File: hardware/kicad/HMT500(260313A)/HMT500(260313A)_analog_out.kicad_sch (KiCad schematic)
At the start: 35 parts, among them U10 TPS26611DDFR, U12 OPA197IDBVR, U13 OPA197IDBVR, U14 SN74LVC2G32DCUR, U7 DAC8760IPWP, U8 DAC8760IPWP, U9 TPS26611DDFR

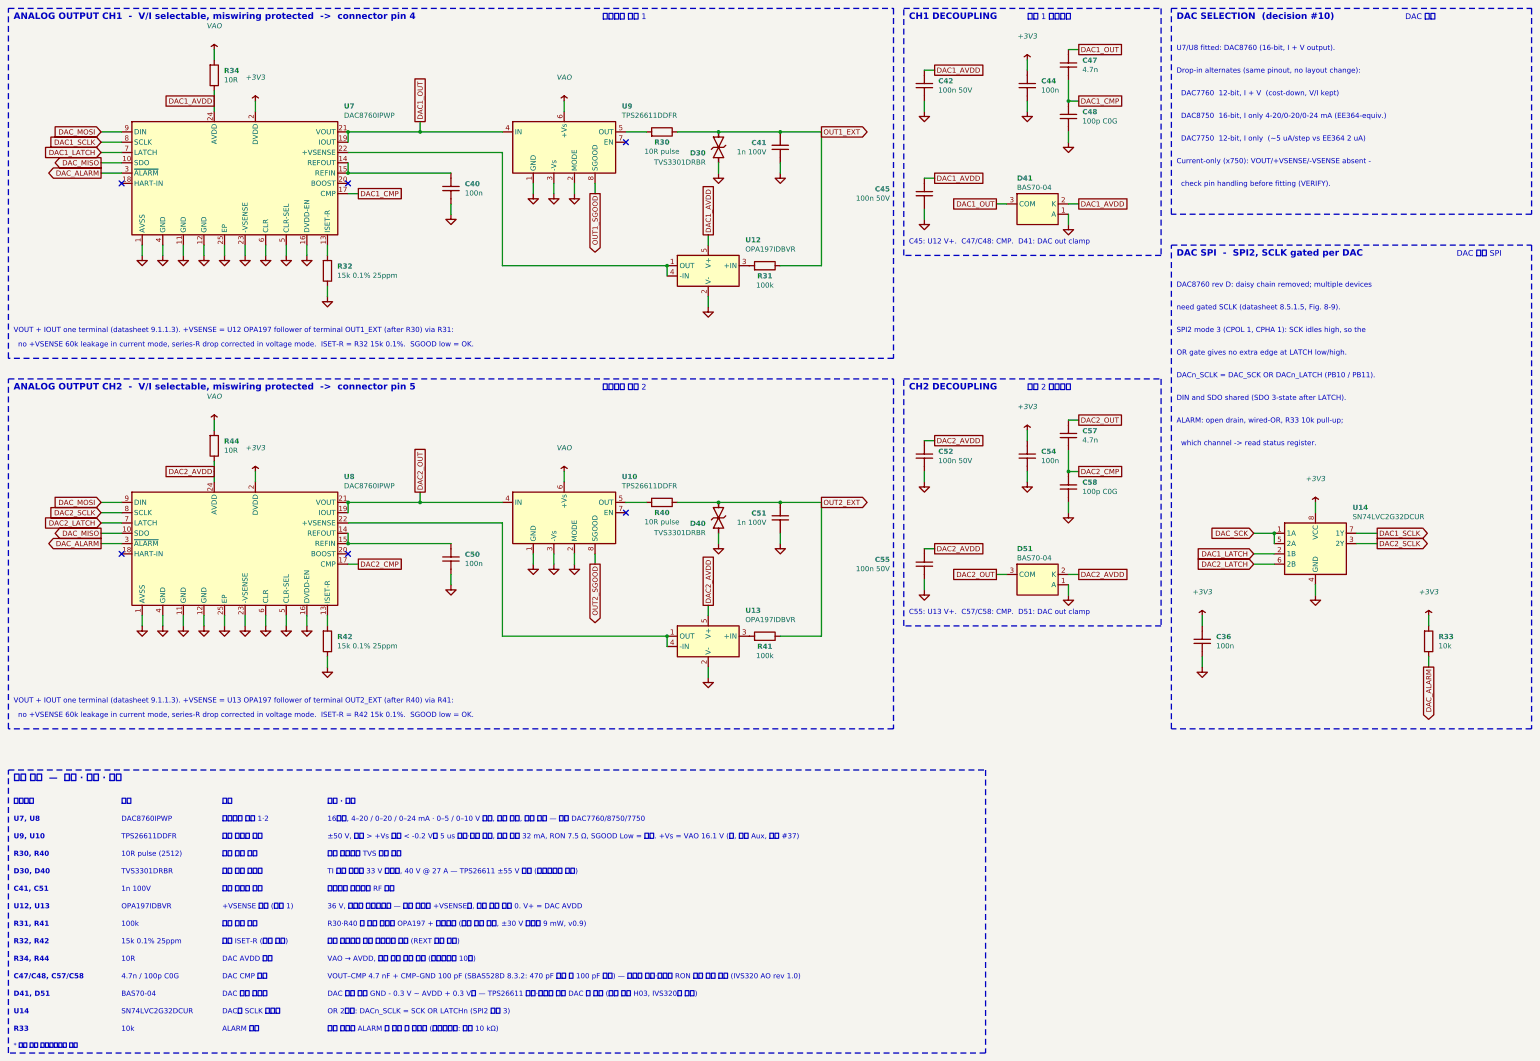
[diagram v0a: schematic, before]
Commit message: 회로 v0.10: AO D30/D40을 TVS1401 14 V로 변경
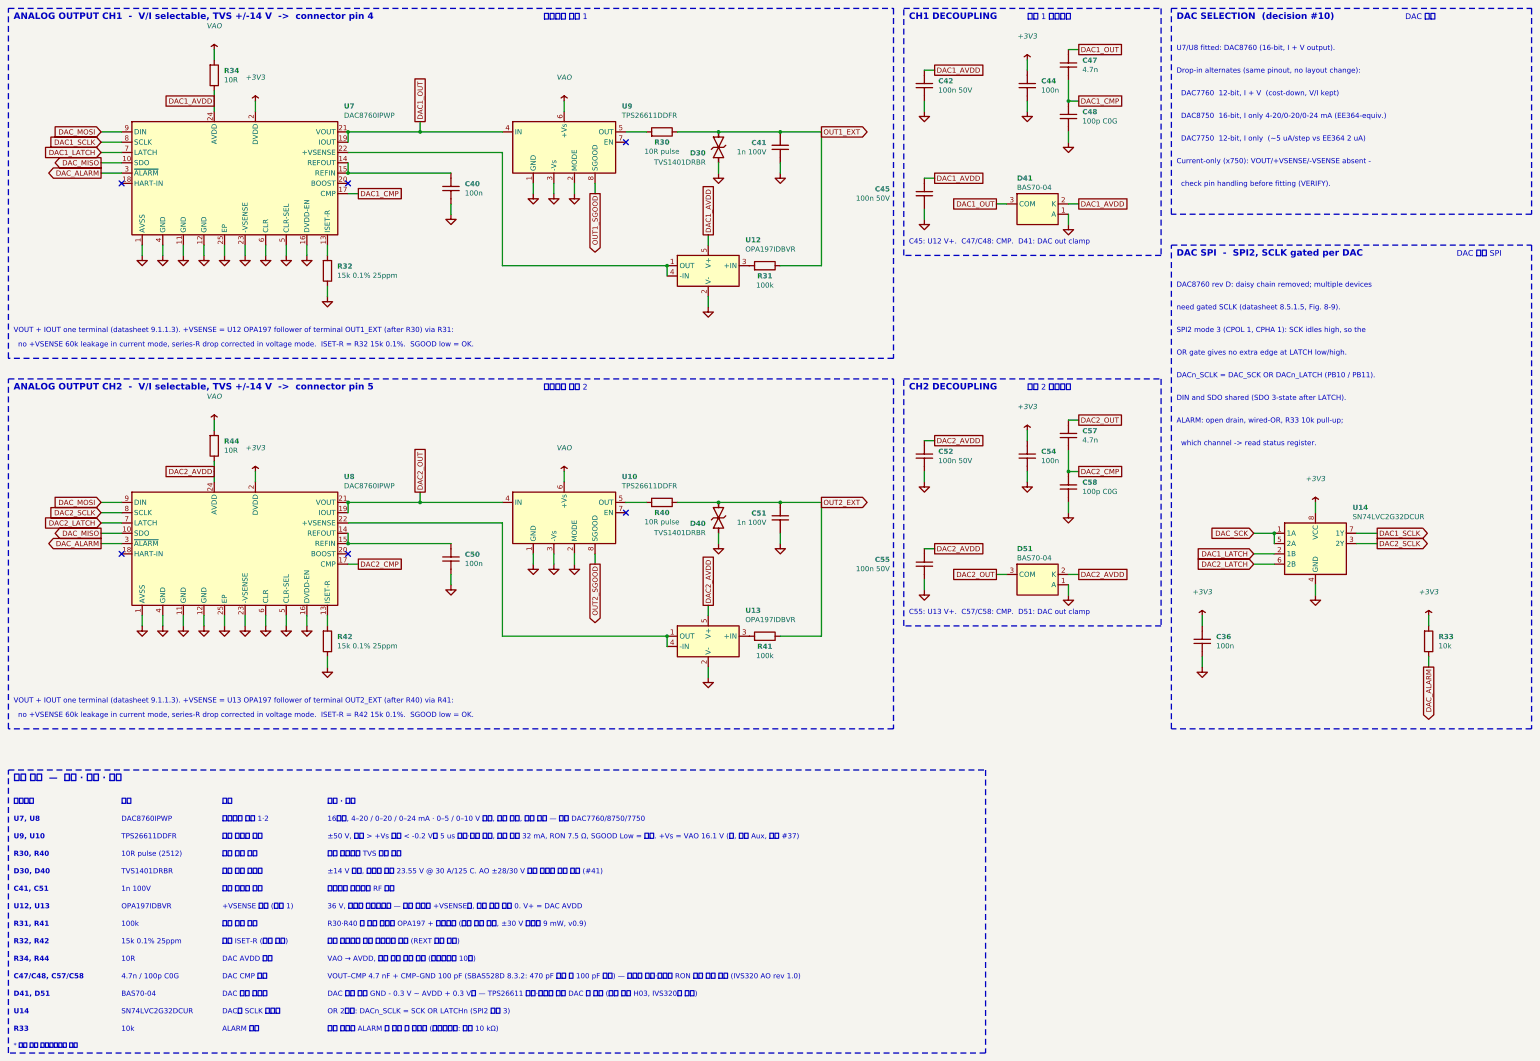
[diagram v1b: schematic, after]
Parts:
- D30, D40: value TVS3301DRBR -> TVS1401DRBR; symbol HMT500_260313A:TVS3301 -> HMT500_260313A:TVS1401
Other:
- note added: "ANALOG OUTPUT CH1 - V/I selectable, TVS +/-14 V -> connector pin 4"
- note added: "ANALOG OUTPUT CH2 - V/I selectable, TVS +/-14 V -> connector pin 5"
- note added: "TVS1401DRBR"
- note added: "±14 V 동작, 클램프 최대 23.55 V @ 30 A/125 C. AO ±28/30 V 지속 오결선 보장 제외 (#41)"
- note removed: "ANALOG OUTPUT CH1 - V/I selectable, miswiring protected -> connector pin 4"
- note removed: "ANALOG OUTPUT CH2 - V/I selectable, miswiring protected -> connector pin 5"
- note removed: "TI 평탄 클램프 33 V 양방향, 40 V @ 27 A — TPS26611 ±55 V 보호 (데이터시트 권장)"
- note removed: "TVS3301DRBR"

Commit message: Add HMT500 A1 routing draft and correct SMNR4020 land patterns
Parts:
- C36, C40, C44, C47, C48, C50, C54, C57, C58: footprint Capacitor_SMD:C_0402_1005Metric -> HMT500_260313A:C_0402_1005Metric
- C41, C51: footprint Capacitor_SMD:C_0603_1608Metric -> HMT500_260313A:C_0603_1608Metric
- C42, C45, C52, C55: footprint Capacitor_SMD:C_0805_2012Metric -> HMT500_260313A:C_0805_2012Metric
- D41, D51: footprint Package_TO_SOT_SMD:SOT-23 -> HMT500_260313A:SOT-23
- R30, R40: footprint Resistor_SMD:R_2512_6332Metric -> HMT500_260313A:R_2512_6332Metric
- R31, R33, R34, R41, R44: footprint Resistor_SMD:R_0402_1005Metric -> HMT500_260313A:R_0402_1005Metric
- R32, R42: footprint Resistor_SMD:R_0603_1608Metric -> HMT500_260313A:R_0603_1608Metric
- U10, U9: footprint Package_TO_SOT_SMD:SOT-23-8 -> HMT500_260313A:SOT-23-8
- U12, U13: footprint Package_TO_SOT_SMD:SOT-23-5 -> HMT500_260313A:SOT-23-5
- U14: footprint Package_SO:VSSOP-8_2.3x2mm_P0.5mm -> HMT500_260313A:VSSOP-8_2.3x2mm_P0.5mm
- U7, U8: footprint Package_SO:HTSSOP-24-1EP_4.4x7.8mm_P0.65mm_EP3.2x5mm -> HMT500_260313A:HTSSOP-24-1EP_4.4x7.8mm_P0.65mm_EP3.2x5mm
